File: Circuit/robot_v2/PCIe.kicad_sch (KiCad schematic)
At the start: 15 parts, among them J12 10018783-11200TLF, U10 AP64501SP-13

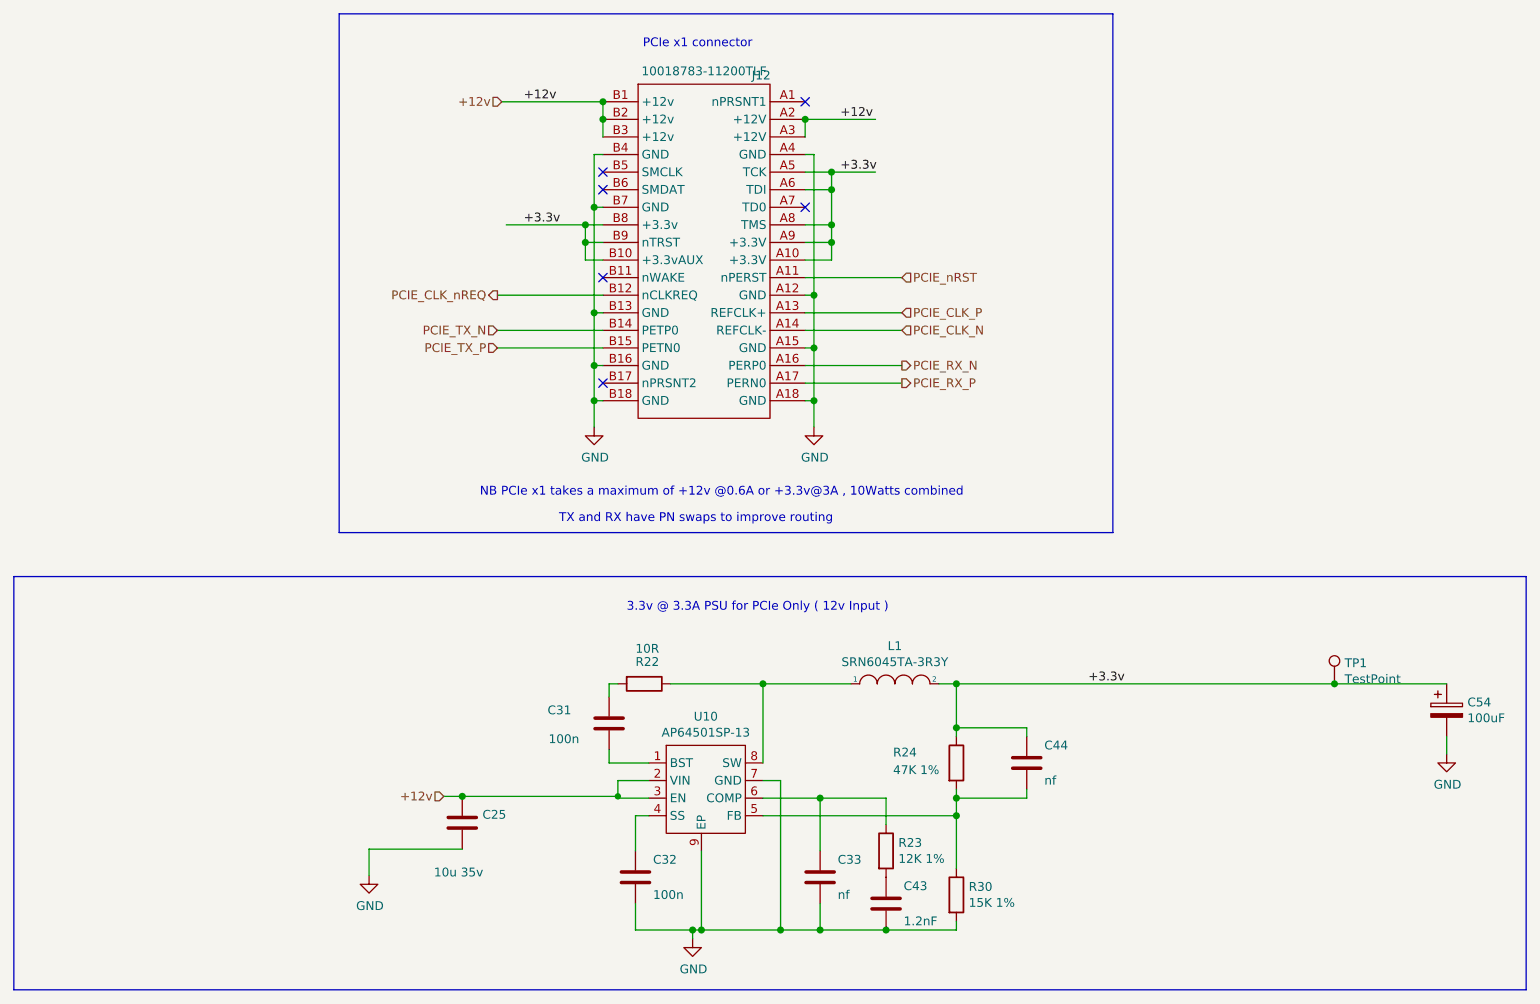
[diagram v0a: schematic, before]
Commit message: feat(kicad): Advance PCB to v0.3 and add EV3 color sensor test
Updates the main robot PCB design to version 0.3 ('Robot fő nyák_v3') with new features and refinements. Simultaneously adds a v0.1 test program for the Lego EV3 color sensor.
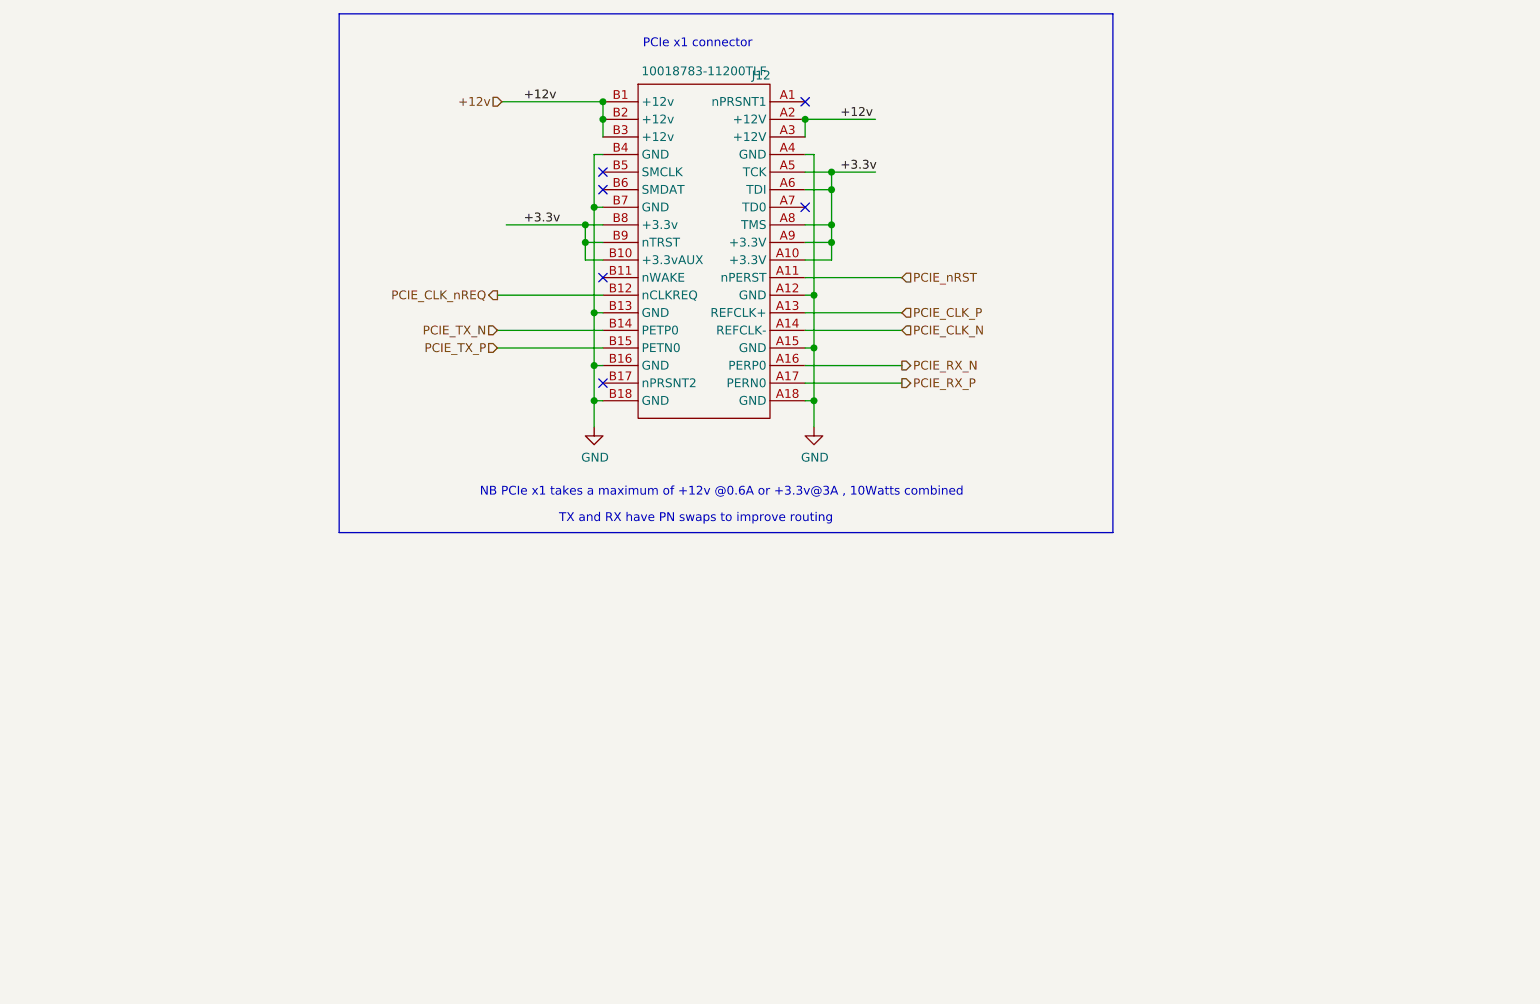
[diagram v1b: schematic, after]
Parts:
- removed C25: 10u 35v, Capacitor_SMD:C_0805_2012Metric, symbol Device:C
- removed C31, C32: 100n, Capacitor_SMD:C_0805_2012Metric, symbol Device:C
- removed C33, C44: nf, Capacitor_SMD:C_0805_2012Metric, symbol Device:C
- removed C43: 1.2nF, Capacitor_SMD:C_0805_2012Metric, symbol Device:C
- removed C54: 100uF, Capacitor_Tantalum_SMD:CP_EIA-7343-31_Kemet-D, symbol Device:CP
- removed L1: SRN6045TA-3R3Y, Inductor_SMD:L_Bourns_SRN6045TA, symbol pspice:INDUCTOR
- removed R22: 10R, Resistor_SMD:R_0805_2012Metric_Pad1.20x1.40mm_HandSolder, symbol Device:R
- removed R23: 12K 1%, Resistor_SMD:R_0805_2012Metric_Pad1.20x1.40mm_HandSolder, symbol Device:R
- removed R24: 47K 1%, Resistor_SMD:R_0805_2012Metric_Pad1.20x1.40mm_HandSolder, symbol Device:R
- removed R30: 15K 1%, Resistor_SMD:R_0805_2012Metric_Pad1.20x1.40mm_HandSolder, symbol Device:R
- removed TP1: TestPoint, TestPoint:TestPoint_Pad_1.0x1.0mm, symbol Connector:TestPoint
- removed U10: AP64501SP-13, Package_SO:SOIC-8-1EP_3.9x4.9mm_P1.27mm_EP2.95x4.9mm_Mask2.71x3.4mm_ThermalVias, symbol CM4IO:AP64351
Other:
- note removed: "3.3v @ 3.3A PSU for PCIe Only ( 12v Input )"
